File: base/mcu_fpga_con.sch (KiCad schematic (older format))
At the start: 2 parts, among them J14 Conn_02x25_Odd_Even, J15 Conn_02x25_Odd_Even

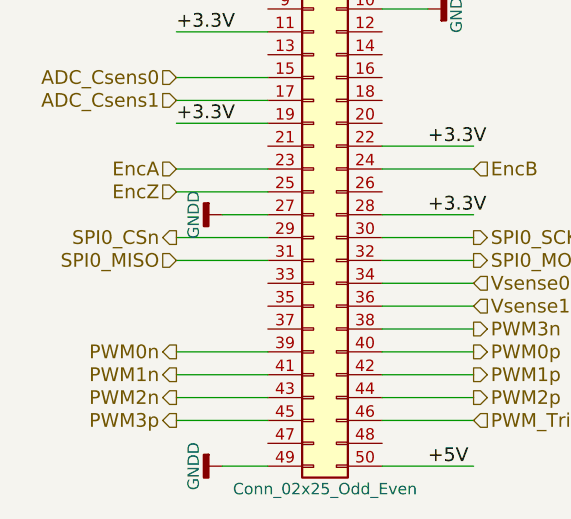
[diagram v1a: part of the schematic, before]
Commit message: Update base board: 1. Add extra analog voltage input to core board.   -> update pinmux 2. Assign most footprints. 3. Generate netlist. 4. Add core_sf board. 5. Add kicad_symbols library submodule.
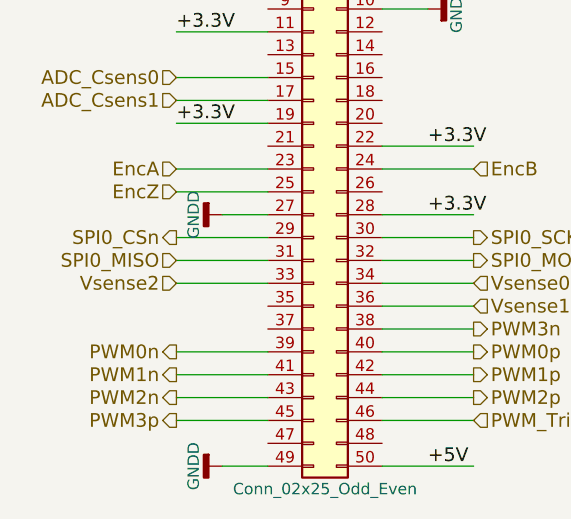
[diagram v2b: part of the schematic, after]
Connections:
- net labels added: Vsense2
- wire segments 54 -> 55
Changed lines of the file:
@@
 	10300 1300 10300 1400
 $Comp
-L GNDD #PWR17
+L GNDD #PWR014
 U 1 1 5A2BBBBD
 P 10300 1400
-F 0 "#PWR17" H 10300 1150 50  0001 C CNN
+F 0 "#PWR014" H 10300 1150 50  0001 C CNN
 F 1 "GNDD" H 10300 1275 50  0000 C CNN
 F 2 "" H 10300 1400 50  0001 C CNN
@@
 	4300 1800 4500 1800
 $Comp
-L GNDD #PWR13
+L GNDD #PWR015
 U 1 1 5A2BBDBA
 P 3600 3800
-F 0 "#PWR13" H 3600 3550 50  0001 C CNN
+F 0 "#PWR015" H 3600 3550 50  0001 C CNN
 F 1 "GNDD" H 3600 3675 50  0000 C CNN
 F 2 "" H 3600 3800 50  0001 C CNN
@@
 $EndComp
 $Comp
-L GNDD #PWR12
+L GNDD #PWR016
 U 1 1 5A2BBDD1
 P 3600 2700
-F 0 "#PWR12" H 3600 2450 50  0001 C CNN
+F 0 "#PWR016" H 3600 2450 50  0001 C CNN
 F 1 "GNDD" H 3600 2575 50  0000 C CNN
 F 2 "" H 3600 2700 50  0001 C CNN
@@
 $EndComp
 $Comp
-L GNDD #PWR14
+L GNDD #PWR017
 U 1 1 5A2BBDE2
 P 4500 1800
-F 0 "#PWR14" H 4500 1550 50  0001 C CNN
+F 0 "#PWR017" H 4500 1550 50  0001 C CNN
 F 1 "GNDD" H 4500 1675 50  0000 C CNN
 F 2 "" H 4500 1800 50  0001 C CNN
@@
 	6900 1400 7100 1400
 $Comp
-L GNDD #PWR16
+L GNDD #PWR018
 U 1 1 5A2BC169
 P 7100 1400
-F 0 "#PWR16" H 7100 1150 50  0001 C CNN
+F 0 "#PWR018" H 7100 1150 50  0001 C CNN
 F 1 "GNDD" H 7100 1275 50  0000 C CNN
 F 2 "" H 7100 1400 50  0001 C CNN
@@
 	6400 2700 6200 2700
 $Comp
-L GNDD #PWR15
+L GNDD #PWR019
 U 1 1 5A2BC182
 P 6200 2700
-F 0 "#PWR15" H 6200 2450 50  0001 C CNN
+F 0 "#PWR019" H 6200 2450 50  0001 C CNN
 F 1 "GNDD" H 6200 2575 50  0000 C CNN
 F 2 "" H 6200 2700 50  0001 C CNN
@@
 Wire Wire Line
 	4700 3000 4300 3000
+Text HLabel 3400 3000 0    60   Input ~ 0
+Vsense2
+Wire Wire Line
+	3400 3000 3800 3000
 $EndSCHEMATC

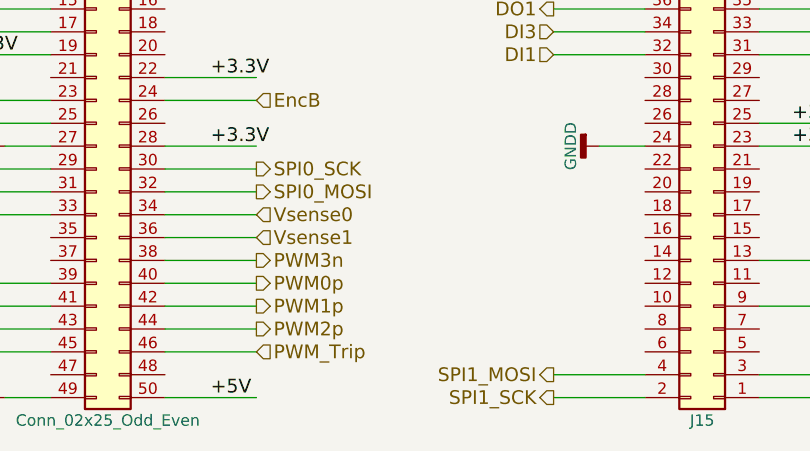
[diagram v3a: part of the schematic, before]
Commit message: some test points
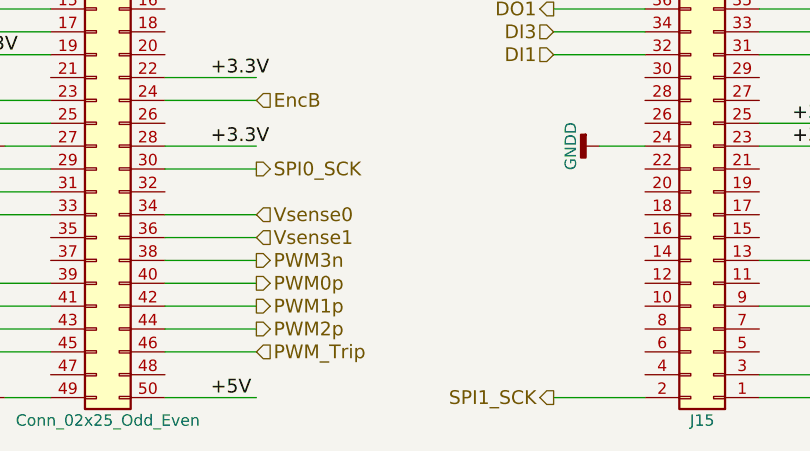
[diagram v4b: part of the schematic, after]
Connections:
- net labels removed: SPI0_MOSI, SPI1_MOSI
- wire segments 55 -> 53
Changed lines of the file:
@@
 Text HLabel 3400 2800 0    60   Output ~ 0
 SPI0_CSn
-Text HLabel 4700 2900 2    60   Output ~ 0
-SPI0_MOSI
 Text HLabel 3400 2900 0    60   Input ~ 0
 SPI0_MISO
@@
 Text HLabel 7300 3800 2    60   Output ~ 0
 SPI1_CSn
-Text HLabel 6000 3700 0    60   Output ~ 0
-SPI1_MOSI
 Text HLabel 7300 3700 2    60   Input ~ 0
 SPI1_MISO
@@
 	4700 2800 4300 2800
 Wire Wire Line
-	4700 2900 4300 2900
-Wire Wire Line
 	3800 2500 3400 2500
 Wire Wire Line
@@
 	6400 3800 6000 3800
 Wire Wire Line
-	6400 3700 6000 3700
-Wire Wire Line
 	7300 3800 6900 3800
